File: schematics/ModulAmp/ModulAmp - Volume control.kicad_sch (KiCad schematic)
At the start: 3 parts, among them U1 MAX1044

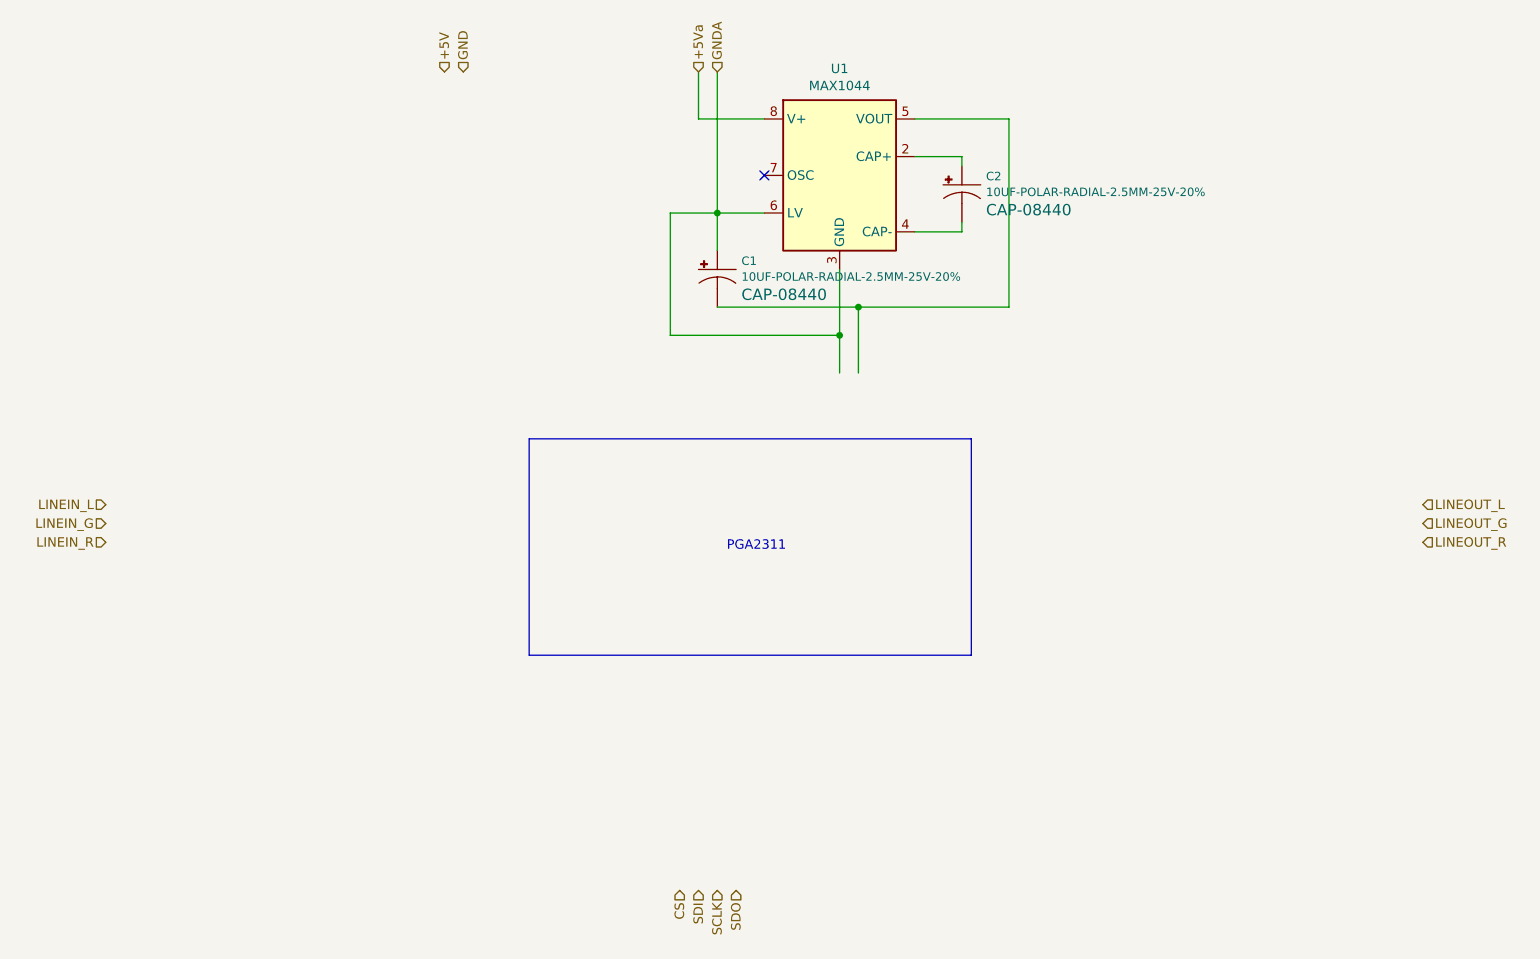
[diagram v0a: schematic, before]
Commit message: Refactored strings and added DHTxx full support
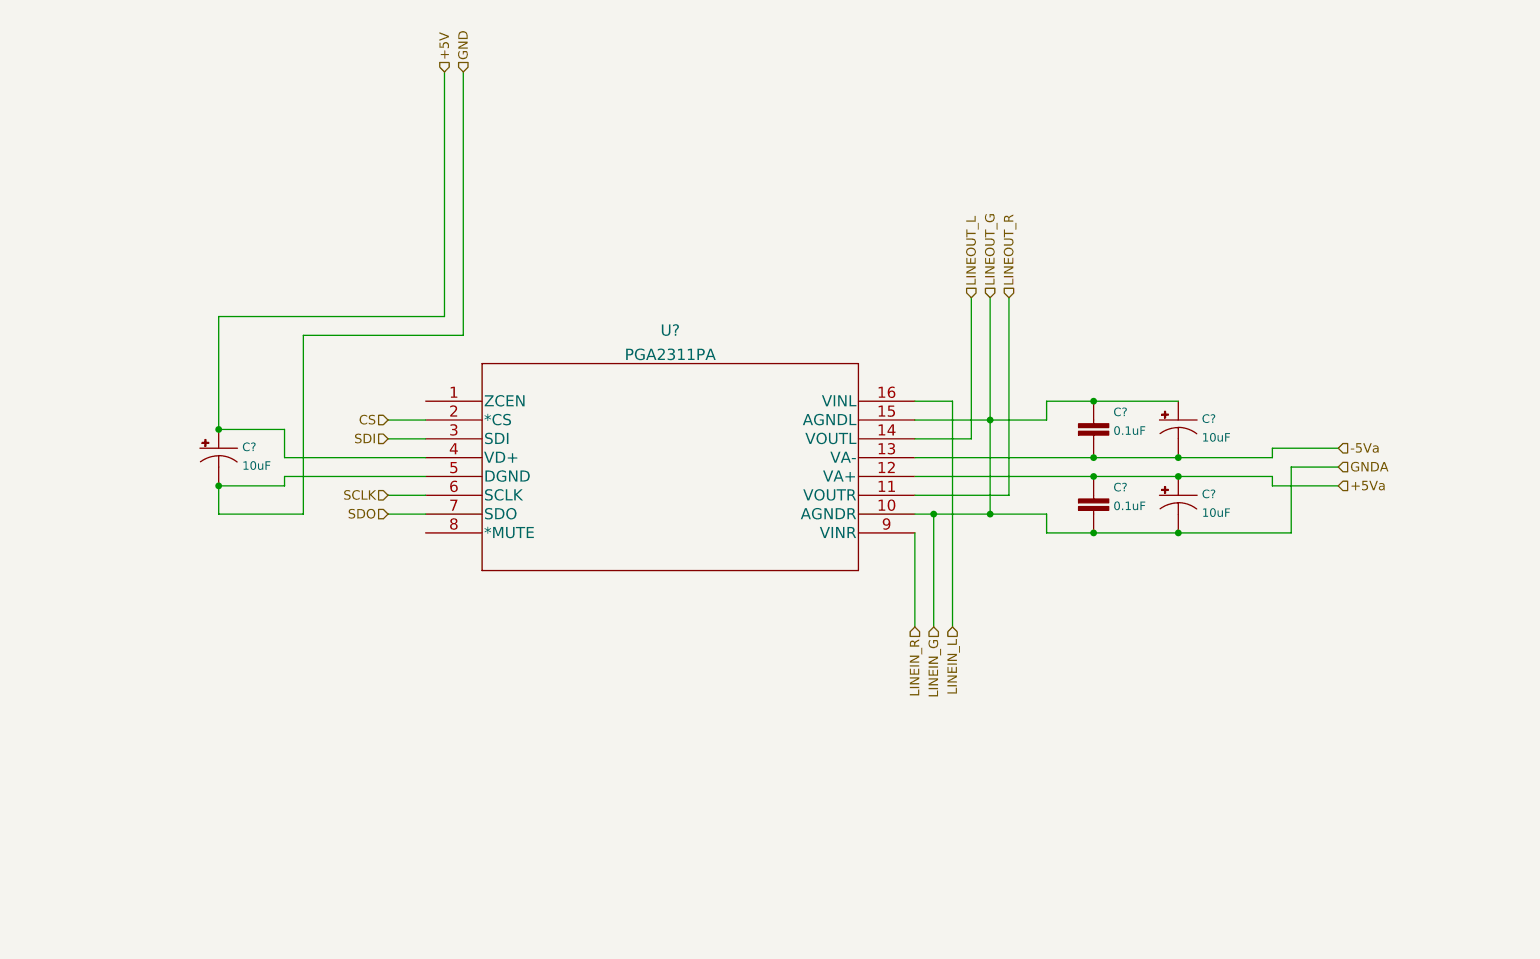
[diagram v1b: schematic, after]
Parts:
- removed C1, C2: 10UF-POLAR-RADIAL-2.5MM-25V-20%, CPOL-RADIAL-2.5MM-5MM, symbol SparkFun-Capacitors:10UF-POLAR-RADIAL-2.5MM-25V-20%
- removed U1: MAX1044, symbol Regulator_SwitchedCapacitor:MAX1044
- added C? (x3): 10uF, CPOL-RADIAL-2.5MM-5MM, symbol SparkFun-Capacitors:10UF-POLAR-RADIAL-2.5MM-25V-20%
- added C? (x2): 0.1uF, 0402, symbol SparkFun-Capacitors:0.1UF-0402-16V-10%
- added U?: PGA2311PA, N16, symbol pga2311:PGA2311PA
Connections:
- net +5V: now also C?.1 (+), U?.4 (VD+)
- net +5Va: now also C?.1, C?.1 (+), U?.12 (VA+)
- net CS: now also U?.2 (*CS)
- net GND: now also C?.2 (-), U?.5 (DGND)
- net GNDA: now also C?.1, C?.1 (+), C?.2, C?.2 (-), U?.10 (AGNDR), U?.15 (AGNDL)
- net LINEIN_L: now also U?.16 (VINL)
- net LINEIN_R: now also U?.9 (VINR)
- net LINEOUT_L: now also U?.14 (VOUTL)
- net LINEOUT_R: now also U?.11 (VOUTR)
- net SCLK: now also U?.6 (SCLK)
- net SDI: now also U?.3 (SDI)
- net SDO: now also U?.7 (SDO)
- new net -5Va: C?.2, C?.2 (-), U?.13 (VA-)
- no-connect marks 1 -> 0
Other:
- note removed: "PGA2311"
